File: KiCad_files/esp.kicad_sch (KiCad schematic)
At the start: 14 parts, among them J2 USB_C_Receptacle_USB2.0_16P, SW1 SW_Push, U1 ESP32-S3-MINI-1U, U2 BNO055

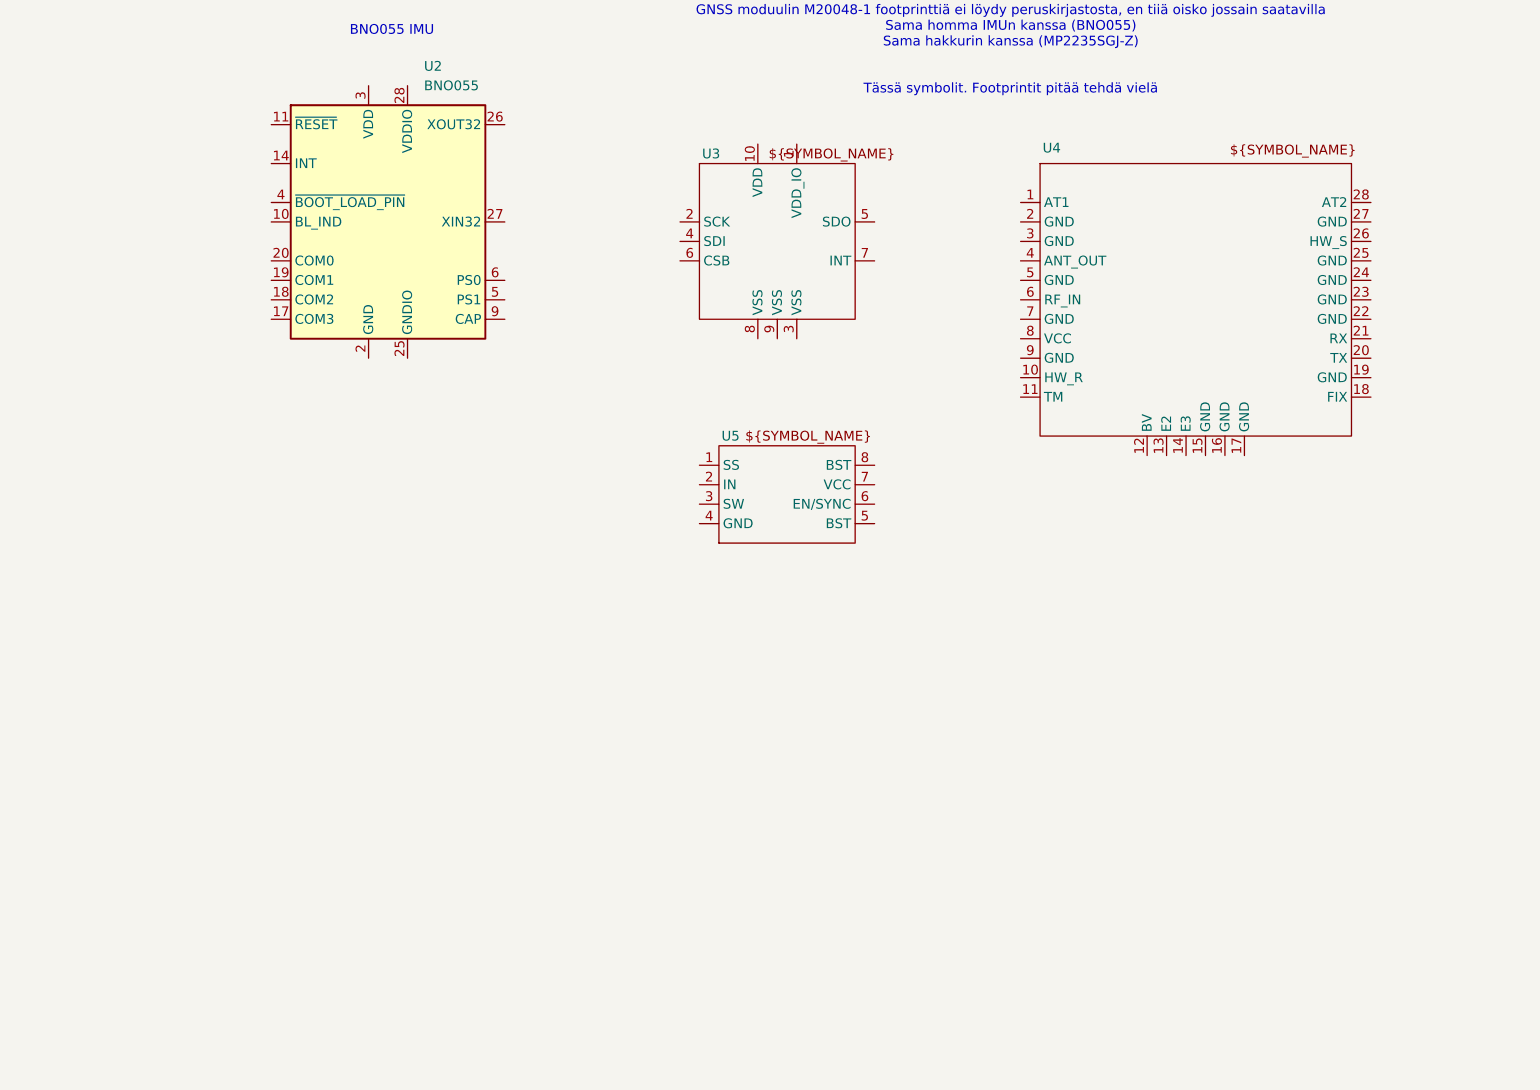
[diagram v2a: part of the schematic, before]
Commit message: Pari komponenttia powerille
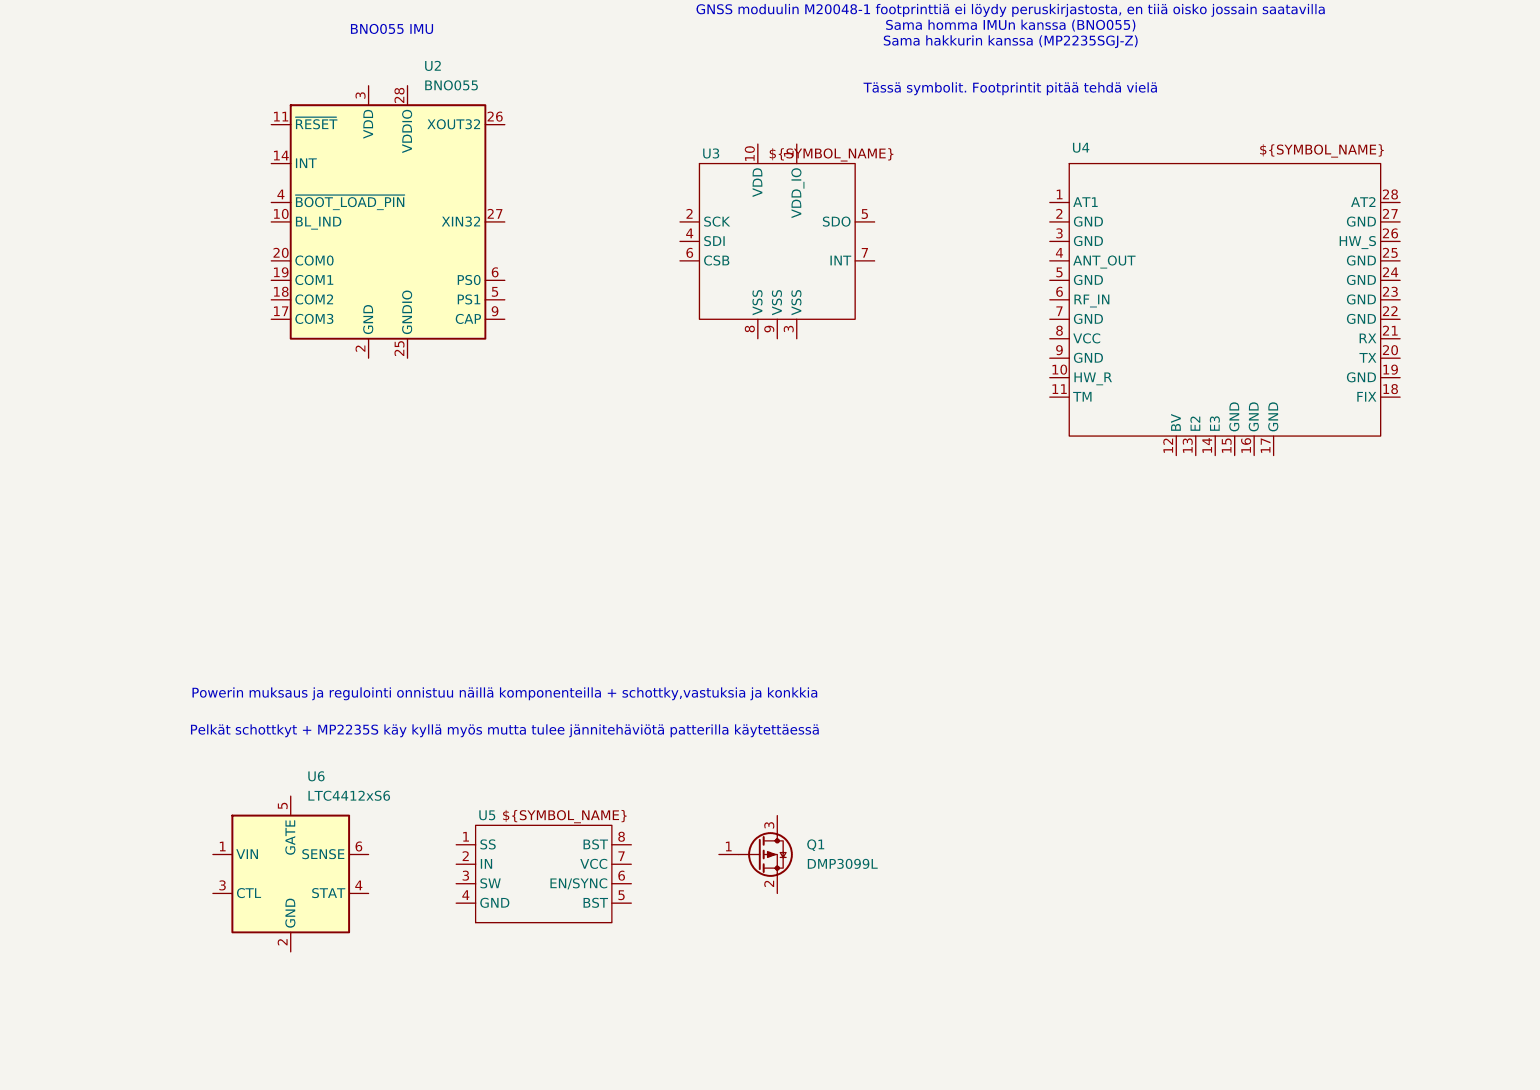
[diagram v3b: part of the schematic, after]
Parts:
- added Q1: DMP3099L, Package_TO_SOT_SMD:SOT-23, symbol Transistor_FET:DMP3099L
- added U6: LTC4412xS6, Package_TO_SOT_SMD:TSOT-23-6, symbol Power_Management:LTC4412xS6
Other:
- note added: "Pelkät schottkyt + MP2235S käy kyllä myös mutta tulee jännitehäviötä patterilla käytettäessä"
- note added: "Powerin muksaus ja regulointi onnistuu näillä komponenteilla + schottky,vastuksia ja konkkia"
- moved on the sheet: U4, U5
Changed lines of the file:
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@@
 	(generator_version "9.0")
 	(paper "A3")
+	(text "Pelkät schottkyt + MP2235S käy kyllä myös mutta tulee jännitehäviötä patterilla käytettäessä"
+		(exclude_from_sim no)
+		(at 80.01 132.588 0)
+		(effects
+			(font
+				(size 1.27 1.27)
+			)
+		)
+	)
 	(text "BNO055 IMU"
 		(exclude_from_sim no)
@@
 		(exclude_from_sim no)
 		(at 66.548 249.936 0)
+		(effects
+			(font
+				(size 1.27 1.27)
+			)
+		)
+	)
+	(text "Powerin muksaus ja regulointi onnistuu näillä komponenteilla + schottky,vastuksia ja konkkia"
+		(exclude_from_sim no)
+		(at 80.01 127.762 0)
 		(effects
 			(font
@@
 	)
 	(symbol
+		(lib_id "Transistor_FET:DMP3099L")
+		(at 113.03 148.59 0)
+		(unit 1)
+		(exclude_from_sim no)
+		(in_bom yes)
+		(on_board yes)
+		(dnp no)
+		(fields_autoplaced yes)
+		(property "Reference" "Q1"
+			(at 119.38 147.3199 0)
+			(effects
+				(font
+					(size 1.27 1.27)
+				)
+				(justify left)
+			)
+		)
+		(property "Value" "DMP3099L"
+			(at 119.38 149.8599 0)
+			(effects
+				(font
+					(size 1.27 1.27)
+				)
+				(justify left)
+			)
+		)
+		(property "Footprint" "Package_TO_SOT_SMD:SOT-23"
+			(at 118.11 150.495 0)
+			(effects
+				(font
+					(size 1.27 1.27)
+					(italic yes)
+				)
+				(justify left)
+				(hide yes)
+			)
+		)
+		(property "Datasheet" "https://www.diodes.com/assets/Datasheets/DMP3099L.pdf"
+			(at 118.11 152.4 0)
+			(effects
+				(font
+					(size 1.27 1.27)
+				)
+				(justify left)
+				(hide yes)
+			)
+		)
+		(property "Description" "-3.8A Id, -30V Vds, P-Channel MOSFET, SOT-23"
+			(at 113.03 148.59 0)
+			(effects
+				(font
+					(size 1.27 1.27)
+				)
+				(hide yes)
+			)
+		)
+		(pin "2"
+		)
+		(pin "1"
+		)
+		(pin "3"
+		)
+		(instances
+			(project ""
+				(path "/186d5500-054c-4b47-a89c-85f6ce2abe33"
+					(reference "Q1")
+					(unit 1)
+				)
+			)
+		)
+	)
+	(symbol
 		(lib_id "Device:R")
 		(at 67.31 233.68 0)
@@
 	)
 	(symbol
+		(lib_id "Power_Management:LTC4412xS6")
+		(at 52.07 151.13 0)
+		(unit 1)
+		(exclude_from_sim no)
+		(in_bom yes)
+		(on_board yes)
+		(dnp no)
+		(fields_autoplaced yes)
+		(property "Reference" "U6"
+			(at 54.2133 138.43 0)
+			(effects
+				(font
+					(size 1.27 1.27)
+				)
+				(justify left)
+			)
+		)
+		(property "Value" "LTC4412xS6"
+			(at 54.2133 140.97 0)
+			(effects
+				(font
+					(size 1.27 1.27)
+				)
+				(justify left)
+			)
+		)
+		(property "Footprint" "Package_TO_SOT_SMD:TSOT-23-6"
+			(at 68.58 160.02 0)
+			(effects
+				(font
+					(size 1.27 1.27)
+				)
+				(hide yes)
+			)
+		)
+		(property "Datasheet" "https://www.analog.com/media/en/technical-documentation/data-sheets/4412fb.pdf"
+			(at 105.41 156.21 0)
+			(effects
+				(font
+					(size 1.27 1.27)
+				)
+				(hide yes)
+			)
+		)
+		(property "Description" "Low Loss PowerPath Controller, TSOT-23-6"
+			(at 52.07 151.13 0)
+			(effects
+				(font
+					(size 1.27 1.27)
+				)
+				(hide yes)
+			)
+		)
+		(pin "5"
+		)
+		(pin "4"
+		)
+		(pin "1"
+		)
+		(pin "3"
+		)
+		(pin "2"
+		)
+		(pin "6"
+		)
+		(instances
+			(project ""
+				(path "/186d5500-054c-4b47-a89c-85f6ce2abe33"
+					(reference "U6")
+					(unit 1)
+				)
+			)
+		)
+	)
+	(symbol
 		(lib_id "power:GND")
 		(at 67.31 238.76 0)
@@
 	(symbol
 		(lib_id "1_projektin osat:M20048-1")
-		(at 149.86 58.42 0)
+		(at 153.67 58.42 0)
 		(unit 1)
 		(exclude_from_sim no)
@@
 		(dnp no)
 		(property "Reference" "U4"
-			(at 151.384 56.388 0)
+			(at 155.194 56.388 0)
 			(effects
 				(font
@@
 		)
 		(property "Value" "~"
-			(at 149.86 58.42 0)
+			(at 153.67 58.42 0)
 			(effects
 				(font
@@
 		)
 		(property "Footprint" ""
-			(at 149.86 58.42 0)
+			(at 153.67 58.42 0)
 			(effects
 				(font
@@
 		)
 		(property "Datasheet" ""
-			(at 149.86 58.42 0)
+			(at 153.67 58.42 0)
 			(effects
 				(font
@@
 		)
 		(property "Description" ""
-			(at 149.86 58.42 0)
+			(at 153.67 58.42 0)
 			(effects
 				(font
@@
 	(symbol
 		(lib_id "1_projektin osat:MP2235S")
-		(at 107.95 95.25 0)
+		(at 76.2 144.78 0)
 		(unit 1)
 		(exclude_from_sim no)
@@
 		(dnp no)
 		(property "Reference" "U5"
-			(at 109.474 93.98 0)
+			(at 77.724 143.51 0)
 			(effects
 				(font
@@
 		)
 		(property "Value" "~"
-			(at 107.95 95.25 0)
+			(at 76.2 144.78 0)
 			(effects
 				(font
@@
 		)
 		(property "Footprint" ""
-			(at 107.95 95.25 0)
+			(at 76.2 144.78 0)
 			(effects
 				(font
@@
 		)
 		(property "Datasheet" ""
-			(at 107.95 95.25 0)
+			(at 76.2 144.78 0)
 			(effects
 				(font
@@
 		)
 		(property "Description" ""
-			(at 107.95 95.25 0)
-			(effects
-				(font
+			(at 76.2 144.78 0)
+			(effects
+				(font

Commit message: konffit kuntoon
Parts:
- added C4: C, symbol Device:C
- added D1: D_Schottky, symbol Device:D_Schottky
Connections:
- net +5V is gone; now on net VBUS: J2.A4 (VBUS), J2.A9 (VBUS), J2.B4 (VBUS), J2.B9 (VBUS)
- net +3.3V: now also U5.7 (VCC)
- net GND: now also U6.2 (GND), C4.2
- net at Q1.1 (G): now also U6.5 (GATE)
- net at Q1.2 (S): now also U5.2 (IN), C4.1, D1.1 (K)
- net +BATT: now reaches Q1.3 (D)
- net +BATT: now also U6.1 (VIN)
- net power_mux: now reaches U6.4 (STAT)
- net VBUS: now reaches U6.6 (SENSE)
- net VBUS: now also D1.2 (A)
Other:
- note added: "To load"
- moved on the sheet: Q1, U5, U6

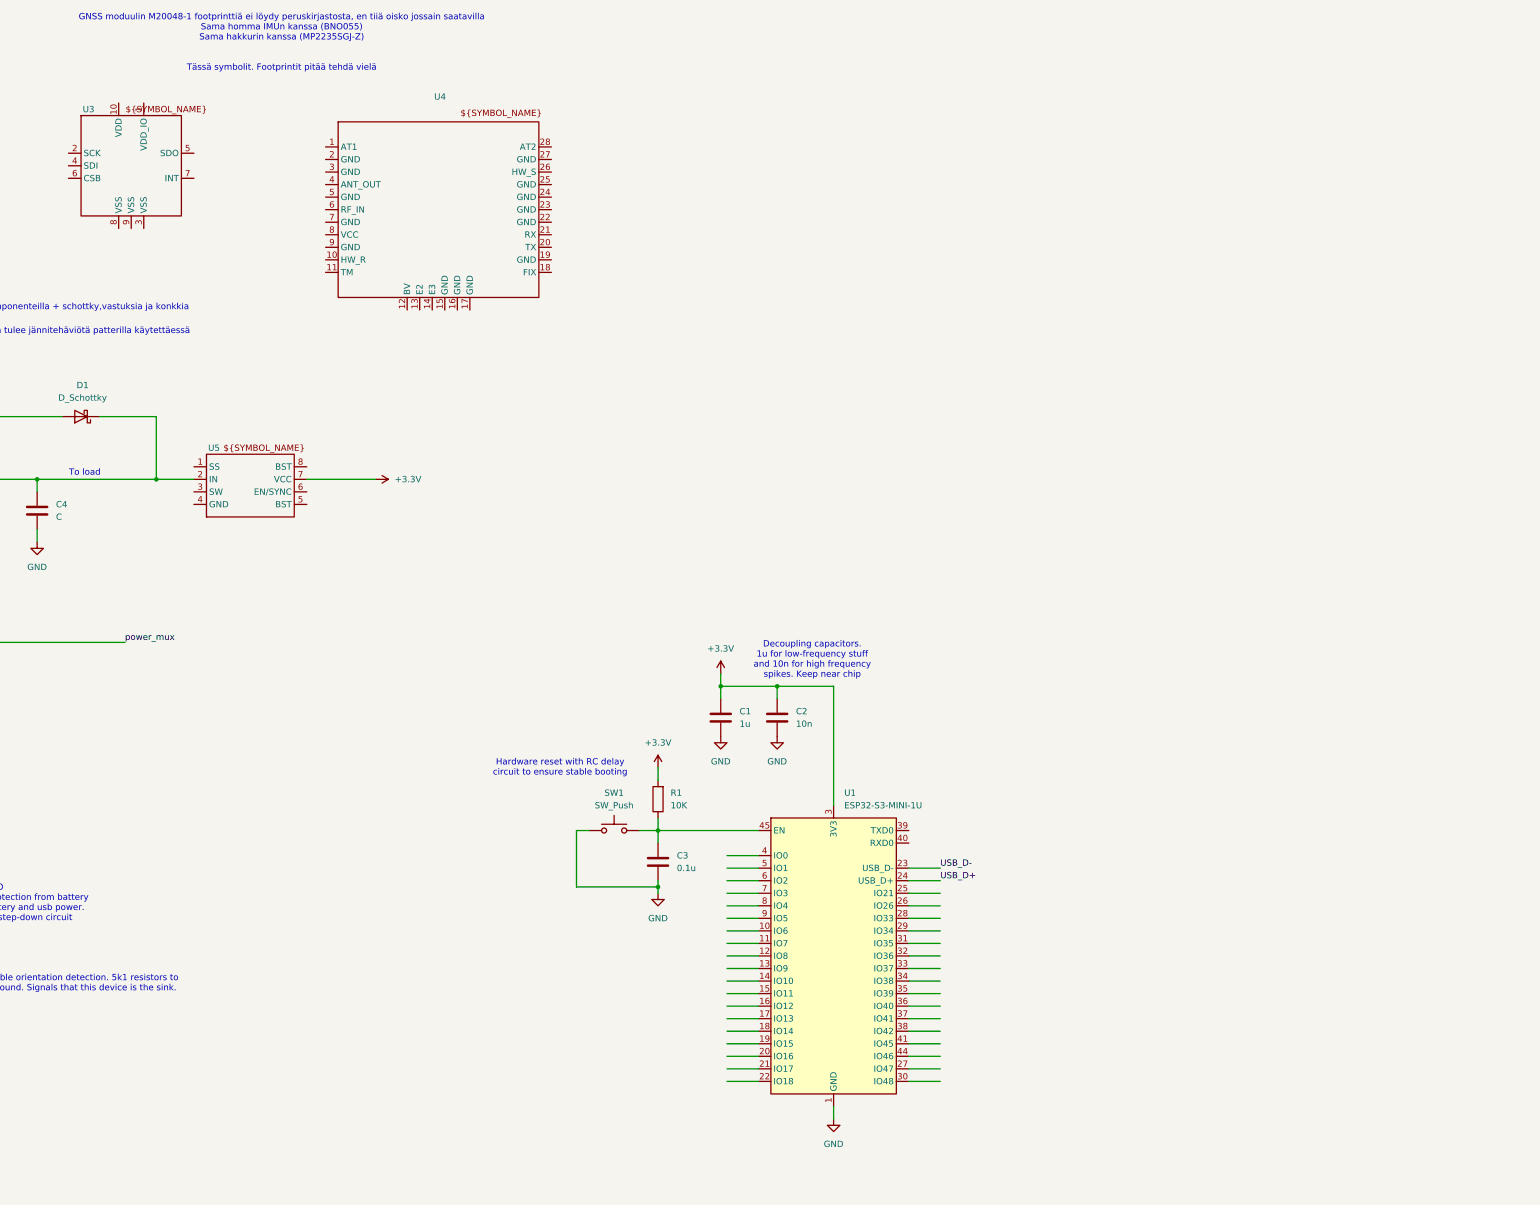
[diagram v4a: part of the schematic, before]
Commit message: hierarchical_sheets
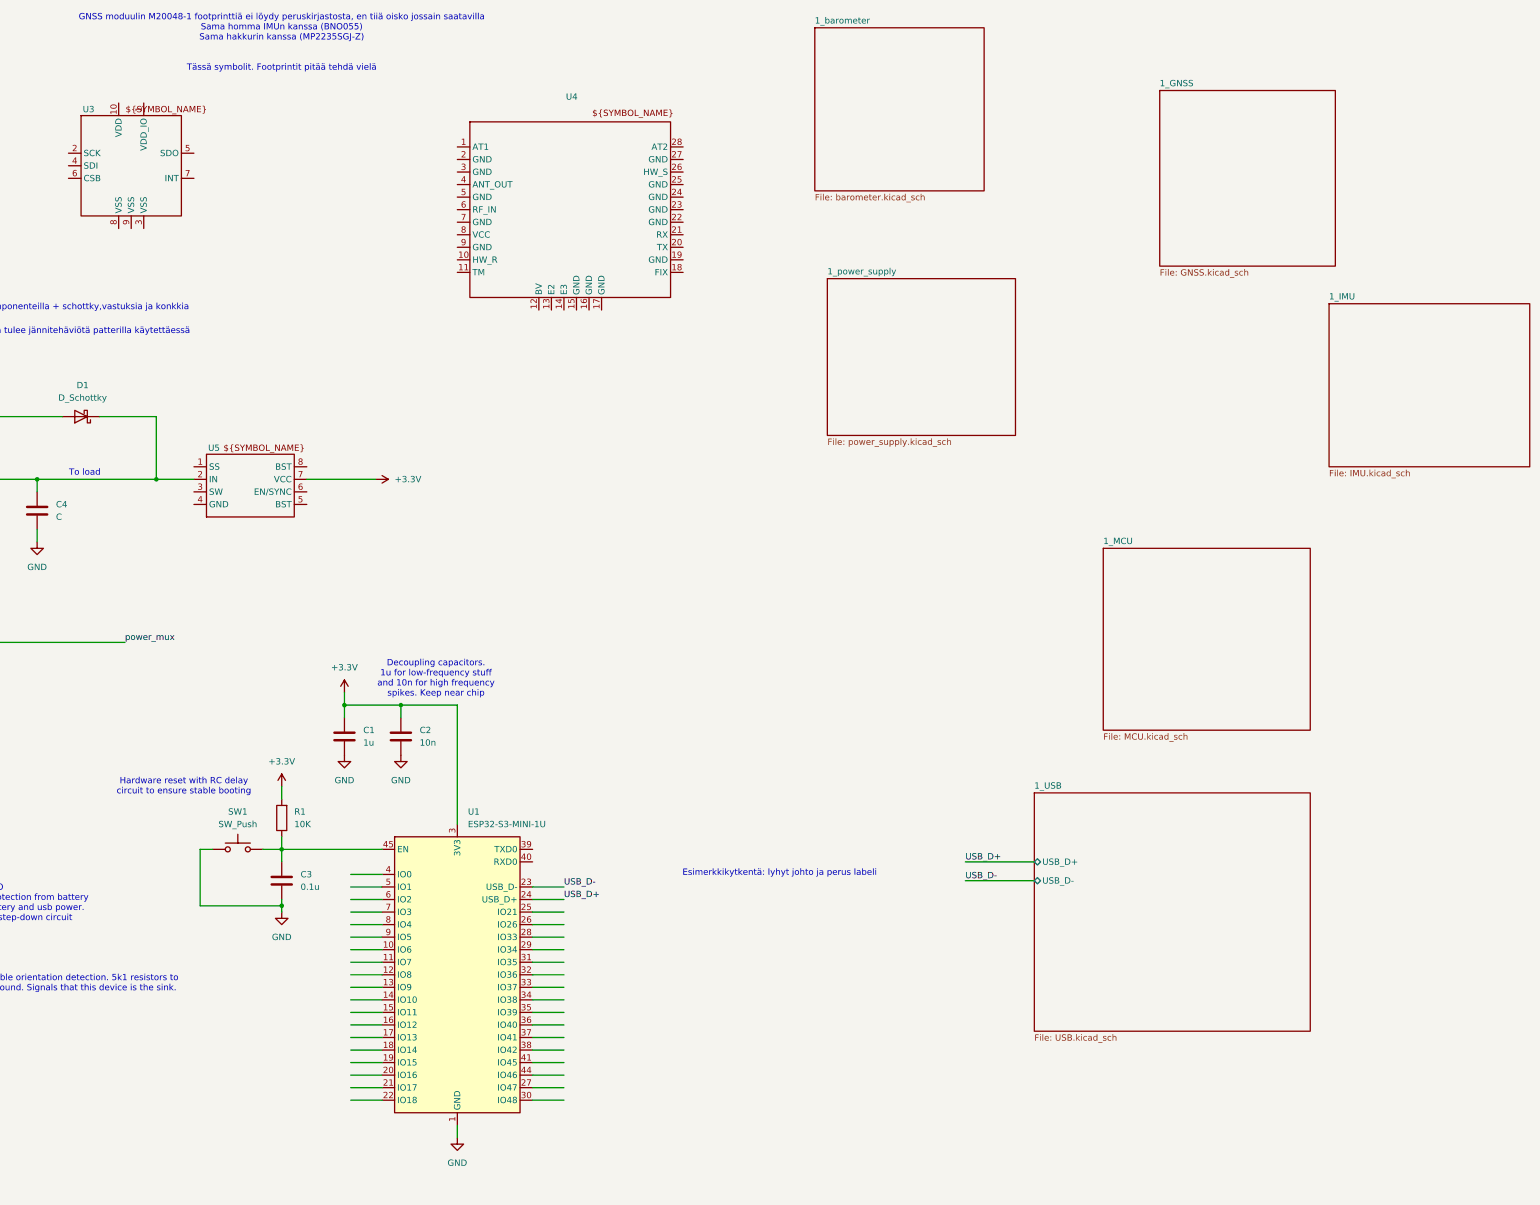
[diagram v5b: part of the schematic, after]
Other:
- added sheet 1_GNSS (GNSS.kicad_sch)
- added sheet 1_IMU (IMU.kicad_sch)
- added sheet 1_MCU (MCU.kicad_sch)
- added sheet 1_USB (USB.kicad_sch)
- added sheet 1_barometer (barometer.kicad_sch)
- added sheet 1_power_supply (power_supply.kicad_sch)
- note added: "Esimerkkikytkentä: lyhyt johto ja perus labeli"
- moved on the sheet: C1, C2, C3, R1, SW1, U1, U4

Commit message: GNSS aloitettu
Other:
- sheet 1_MCU ports: added USB_D+, USB_D-; removed none
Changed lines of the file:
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@@
 	(wire
 		(pts
-			(xy 284.48 209.55) (xy 298.45 209.55)
+			(xy 288.29 209.55) (xy 304.8 209.55)
 		)
 		(stroke
@@
 	(wire
 		(pts
+			(xy 299.72 161.29) (xy 312.42 161.29)
+		)
+		(stroke
+			(width 0)
+			(type default)
+		)
+	)
+	(wire
+		(pts
+			(xy 299.72 156.21) (xy 299.72 157.48)
+		)
+		(stroke
+			(width 0)
+			(type default)
+		)
+	)
+	(wire
+		(pts
+			(xy 312.42 157.48) (xy 299.72 157.48)
+		)
+		(stroke
+			(width 0)
+			(type default)
+		)
+	)
+	(wire
+		(pts
 			(xy 160.02 222.25) (xy 166.37 222.25)
 		)
@@
 	(wire
 		(pts
-			(xy 284.48 213.36) (xy 298.45 213.36)
+			(xy 288.29 213.36) (xy 304.8 213.36)
 		)
 		(stroke
@@
 		)
 	)
+	(label "USB_D-"
+		(at 299.72 161.29 0)
+		(effects
+			(font
+				(size 1.27 1.27)
+			)
+			(justify left bottom)
+		)
+	)
+	(label "USB_D+"
+		(at 288.29 209.55 0)
+		(effects
+			(font
+				(size 1.27 1.27)
+			)
+			(justify left bottom)
+		)
+	)
 	(label "USB_D+"
-		(at 284.48 209.55 0)
+		(at 299.72 156.21 0)
 		(effects
 			(font
@@
 	)
 	(label "USB_D-"
-		(at 284.48 213.36 0)
+		(at 288.29 213.36 0)
 		(effects
 			(font
@@
 			)
 		)
+		(pin "USB_D+" bidirectional
+			(at 312.42 157.48 180)
+			(effects
+				(font
+					(size 1.27 1.27)
+				)
+				(justify left)
+			)
+		)
+		(pin "USB_D-" bidirectional
+			(at 312.42 161.29 180)
+			(effects
+				(font
+					(size 1.27 1.27)
+				)
+				(justify left)
+			)
+		)
 		(instances
 			(project "esp"
@@
 	)
 	(sheet
-		(at 298.45 195.58)
+		(at 304.8 195.58)
 		(size 55.88 48.26)
 		(exclude_from_sim no)
@@
 		)
 		(property "Sheetname" "1_USB"
-			(at 298.45 194.8684 0)
+			(at 304.8 194.8684 0)
 			(effects
 				(font
@@
 		)
 		(property "Sheetfile" "USB.kicad_sch"
-			(at 298.45 244.4246 0)
+			(at 304.8 244.4246 0)
 			(effects
 				(font
@@
 		)
 		(pin "USB_D+" bidirectional
-			(at 298.45 209.55 180)
+			(at 304.8 209.55 180)
 			(effects
 				(font
@@
 		)
 		(pin "USB_D-" bidirectional
-			(at 298.45 213.36 180)
+			(at 304.8 213.36 180)
 			(effects
 				(font
